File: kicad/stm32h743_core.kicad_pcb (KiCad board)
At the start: 4 copper layers, 85 x 65 mm, 80 parts, among them J1 GPIO, J2 GPIO, J3 USB_C, J4 SWD, J5 BOOT, J6 5VIN, SW1 NRST_KEY, SW2 USER_KEY, U1 STM32H743ZIT6, U2 TPS54331DDAR, U3 USBLC6-2SC6, X1 8MHz, X2 32.768kHz

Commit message: feat: 执行层策略——SS 电容 C28、DSN 层类约束、飞线预布线改 B.Cu
- 规格/生成器: TPS54331 SS 外接 C28 10nF(TI §7.3.5 内部无软启动)
- 网表门禁: VCAP 单网、3V3_SW 迁移、SS 规则、LED 极性同步
- gen_pcb: 飞线预布线全部改 B.Cu(层策略), 过孔入盘 0.4/0.2, R14 挪位+C48
- pipeline: DSN 按层策略分四类(GND/P3V3/POW5/Default)带 use_layer 约束
- 状态: 层策略门禁首次通过; DRC 25 未连通+7 error, 收敛方案待决策
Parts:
- added C48: 100nF, C_0402_1005Metric, F.Cu at (28.0, 15.5)
- C43: value 10nF -> 100nF
- C60, C61, C62, C63, C64, C65, C66, C67, C68, C69, C70: value C100n -> 100nF
- C71, C72: value C4.7uF -> 4.7uF
- R14: footprint R_0402_1005Metric -> R_0805_2012Metric
- TP6: value PH -> 3V3_SW
- moved R14 5.50 mm to (38.5, 12.0)
- moved C70 4.80 mm to (33.0, 12.6)
- moved C69 4.63 mm to (43.3, 14.8), turned to -66.916 degrees
- moved H1 2.50 mm to (3.50, 33.0)
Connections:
- C24 pad 1: +3V3 -> 3V3_SW
- C25 pad 1: +3V3 -> 3V3_SW
- D9 pad 1: GND -> PB0
- R15 pad 1: +3V3 -> 3V3_SW
- R25 pad 1: PB0 -> +3V3
- TP6 pad 1: PH -> 3V3_SW
- U3 pad 5: +5V -> VBUS
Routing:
- net 3V3_SW: track 2.77 -> 117.0 mm, vias 0 -> 4
- net PF4: track 49.0 -> 147.9 mm
- net PH: track 86.1 -> 11.0 mm, vias 3 -> 0
- net PD6: track 66.3 -> 0.00 mm, vias 2 -> 0
- net BOOT0: track 113.7 -> 51.1 mm, vias 2 -> 0
- net PB11: track 88.8 -> 143.3 mm, vias 2 -> 1
- net PA10: track 54.4 -> 0.00 mm, vias 2 -> 0
- net PD8: track 53.5 -> 0.00 mm, vias 1 -> 0
- net PG9: track 53.2 -> 0.00 mm, vias 1 -> 0
- net PB1: track 52.4 -> 0.00 mm, vias 1 -> 0
- net NRST: track 106.8 -> 55.8 mm, vias 4 -> 3
- net PE0: track 50.3 -> 0.00 mm, vias 2 -> 0
- net PA7: track 49.0 -> 0.00 mm, vias 1 -> 0
- net PB15: track 48.6 -> 0.00 mm, vias 1 -> 0
- net VCAP: track 128.4 -> 80.0 mm, vias 4 -> 5
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
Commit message: wip: 层策略实验B全链路——0 error未能达成, 如实落盘WIP状态与决策点
- 实验 A/B/B2 数据: 等效配置下未连通 18/25/44/54, Freerouting 存在运行间方差
- build_status.json + README 状态改 WIP/NOT FAB-READY (release_gate fail-closed)
- 已知余量: PB10/PB11 相邻入盘过孔 0.1mm、若干 0.13-0.149 近 miss 间距、未连通信号网
- 决策点: 双GND平面 / 严格策略硬磨 / 维持折中 —— 见方法论 §5.3
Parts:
- added C28: 10n, C_0402_1005Metric, F.Cu at (12.5, 15.0)
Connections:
- U2 pad 4: (no net) -> SS
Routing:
- net +3V3: track 400.6 -> 319.7 mm, vias 12 -> 16
- net USB_DP: track 80.5 -> 0.00 mm, vias 4 -> 0
- net NRST: track 55.8 -> 130.1 mm, vias 3 -> 9
- net PD7: track 72.7 -> 0.00 mm, vias 3 -> 0
- net PB13: track 65.2 -> 0.00 mm, vias 2 -> 0
- net PC5: track 64.0 -> 0.00 mm, vias 3 -> 0
- net PA9: track 60.6 -> 0.00 mm, vias 2 -> 0
- net PB14: track 60.1 -> 0.00 mm, vias 3 -> 0
- net PG14: track 58.2 -> 0.00 mm, vias 2 -> 0
- net PA15: track 58.1 -> 0.00 mm, vias 2 -> 0
- net PG12: track 57.9 -> 0.00 mm, vias 3 -> 0
- net PG9: track 0.00 -> 57.9 mm, vias 0 -> 2
- net PA7: track 0.00 -> 57.0 mm, vias 0 -> 3
- net PA1: track 56.8 -> 0.00 mm, vias 2 -> 0
- net PG10: track 56.2 -> 0.00 mm, vias 1 -> 0
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
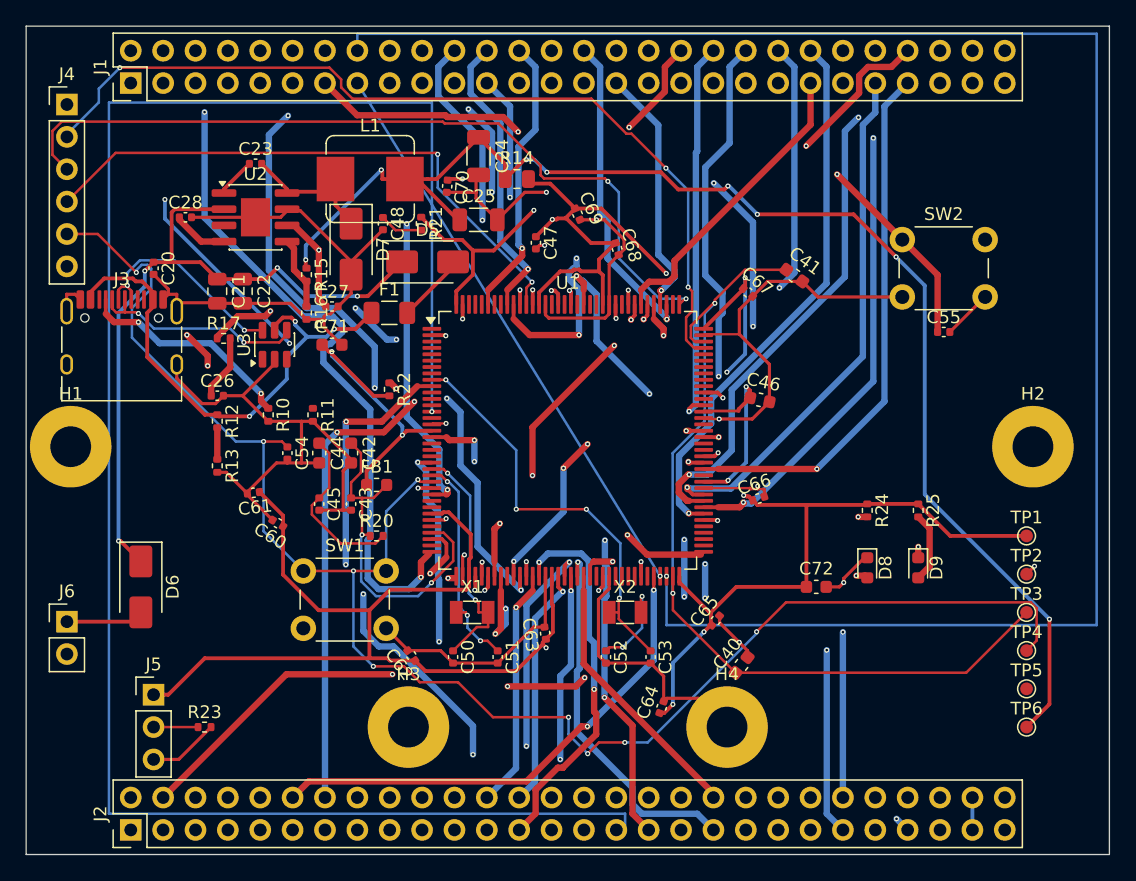
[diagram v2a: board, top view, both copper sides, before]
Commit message: docs+data: 层策略 A/B/B2 实验实录与结构性结论——四层 F/B-only 自动布线不收敛
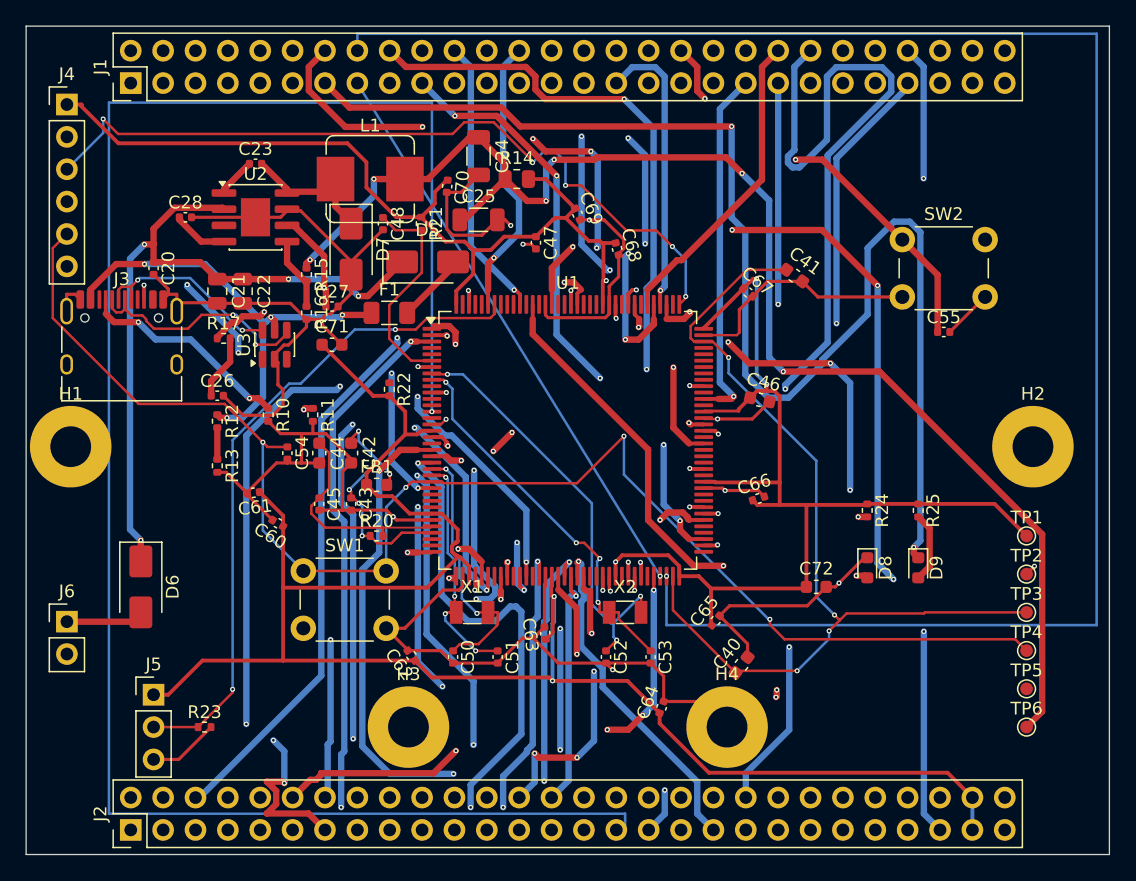
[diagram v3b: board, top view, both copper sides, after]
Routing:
- net PG14: track 0.00 -> 79.9 mm, vias 0 -> 4
- net PE2: track 0.00 -> 70.1 mm, vias 0 -> 5
- net PA13: track 69.8 -> 0.00 mm, vias 3 -> 0
- net PG10: track 0.00 -> 65.6 mm, vias 0 -> 3
- net PG5: track 0.00 -> 62.2 mm, vias 0 -> 4
- net PB13: track 0.00 -> 60.1 mm, vias 0 -> 3
- net PG9: track 57.9 -> 0.00 mm, vias 2 -> 0
- net PA7: track 57.0 -> 0.00 mm, vias 3 -> 0
- net PB12: track 56.7 -> 0.00 mm, vias 3 -> 0
- net PA0: track 56.5 -> 0.00 mm, vias 3 -> 0
- net PG8: track 0.00 -> 56.4 mm, vias 0 -> 2
- net PF8: track 0.00 -> 55.4 mm, vias 0 -> 2
- net PE1: track 0.00 -> 51.0 mm, vias 0 -> 2
- net PG13: track 49.4 -> 0.00 mm, vias 1 -> 0
- net BOOT0: track 3.49 -> 52.5 mm, vias 0 -> 2
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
